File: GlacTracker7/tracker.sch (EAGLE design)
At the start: 79 parts, among them J1 THING_PLUS_PHYSICAL, J5 JST_6_PIN_VERTICAL, Q1 2N3906, Q2 AO6401A, Q3 DMN6070SY, U2 FONA-800-BREAKOUT, U3 MP2155GQ-Z, U4 SPARKFUN-SWARM-M138, U5 SPARKFUN-GPS-ZED-F9P, U6 MP2155GQ-Z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

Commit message: progress
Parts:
- removed J5: JST_6_PIN_VERTICAL, SparkFun-Connectors:JST_6_PIN_VERTICAL
- removed JP4, JP5, JP6, JP7: (no value), jumper:JP2E
- added C21: 1uF, resistor:C-EUC0805
- added JP8: (no value), jumper:JP1Q
- added Q6: MMBT3906LT1SMD, transistor-pnp:MMBT3906LT1SMD
- added Q7, Q8: DMG6602SVT, farnell-parts:DMG6602SVT
- added R20, R21, R23: 100k, SparkFun-Resistors:RESISTOR0603
- added R22, R26: 100K, resistor:R-EU_R0805
- added R24: 200R 0.1%, resistor:R-EU_R0805
- added R25: 1K 0.1%, resistor:R-EU_R0805
- added VCC_S: TPB2,54, testpad:TPB2,54
- Q2: value AO6401A -> DMG6602SVT; device GlacTracker:AO6401A -> farnell-parts:DMG6602SVT
- Q3: value DMN6070SY -> DMG6602SVT; device GlacTracker:DMN6070SY-13 -> farnell-parts:DMG6602SVT
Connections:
- removed net GPS_RX1: J1.A1, U5.RXI/MOSI
- removed net GPS_TX1: J1.A2, U5.TXO/MISO
- removed net GSM_EN: JP11.1, Q3.G, R19.1
- removed net GSM_PS: J1.GPIO0, U2.PS
- removed net GSM_RX: J1.A5, U2.RX
- removed net GSM_TX: J1.GPIO5, U2.TX
- removed net KEY: J1.GPIO1, U2.KEY
- removed net N$16: JP7.2, U6.EN
- removed net N$4: JP5.2, U3.EN
- removed net PSU_EN: J5.3, Q1.C, R2.2
- removed net SWARM_EN: J1.SCK, J5.1
- removed net SWARM_RX: J1.PICO, U4.RXI
- removed net SWARM_TX: J1.POCI, U4.TXO
- removed net VCC1_EN: J1.A0, J5.2, JP7.1
- removed net VCC_1: TP6.1
- new net +3V3: Q7G$2.S, R22.2
- new net ADC_7: C21.1, R24.2, R25.1
- new net BATV_EN: J1.A1
- new net BATV_IN: J1.A0
- new net COMMS_EN: J1.GPIO1, JP8.1, Q3G$1.G, R21.1, U6.EN, U6.MODE/SYNC
- new net COMMS_RX: J1.GPIO0, U2.RX, U4.RXI
- new net COMMS_TX: J1.GPIO5, U2.TX, U4.TXO
- new net GNDA: C21.2, R24.1
- new net GPS_EN: J1.FREE, JP11.1, Q2G$1.G, R19.1
- new net GSM_KEY: J1.GPIO6, U2.KEY
- new net N$35: Q3G$1.D@1, Q3G$2.G, R20.2
- new net SD_CS: J1.A5
- new net SD_MISO: J1.POCI
- new net SD_MOSI: J1.PICO
- new net SD_SCK: J1.SCK
- new net SENSE_3V3: Q7G$2.D, VCC_S.TP
- new net SENSE_EN: Q7G$1.G, Q8G$1.G
- new net SPARE: J1.A4
- new net SPARE2: J1.A3
- new net SPARE3: J1.A2
- new net VCC: Q8G$2.S, R26.2
- new net VCC_HP2_SW1: Q8G$2.D, R25.2
- new net V_COMMS_IO: Q3G$2.D, U2.V_IO
- new net V_GPS: C1.1, C5.1, C7.1, Q2G$2.D, U5.3V3, XB1.VCC
- net 3.3V: now also JP11.2, JP8.2, Q2G$2.S, Q3G$2.S, R18.1, R20.1; no longer C1.1, C5.1, C7.1, U2.V_IO, U5.3V3, XB1.VCC
- net 3V3_EN: now also Q1.C, Q6.C, R2.2, R23.1, U3.EN, U3.MODE/SYNC; no longer JP5.1
- net 4.4V: now also C10.+, C3.1, C9.+, TP6.1, U2.V_BAT, U4.VIN
- net GND: now also Q2G$1.S, Q3G$1.S, Q7G$1.S, Q8G$1.S, R21.2, R23.2; no longer JP4.1, JP6.1, Q3.S
- net N$1: now also Q7G$1.D@1, Q7G$2.G, R22.1; no longer Q1.B, R1.2
- net N$12: now also Q8G$1.D@1, Q8G$2.G, R26.1; no longer JP6.2, U6.MODE/SYNC
- net N$2: now also Q1.B, Q6.B, R1.2; no longer JP4.2, U3.MODE/SYNC
- net N$34: now also Q2G$1.D@1, Q2G$2.G; no longer Q2.G, Q3.D
- net RTC_BAT: now also Q6.E
- net SCL: now also U5.SCL/SCK
- net SDA: now also U5.SDA/!CS
- net V_GSM: no longer C10.+, C9.+, Q2.D, U2.V_BAT
- net V_SWARM: no longer C3.1, U4.VIN
- net V_SYS: no longer JP11.2, JP4.3, JP5.3, JP6.3, JP7.3, Q2.S, R18.1
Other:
- note added: "Bat Measure"
- note added: "GPS Enable"
- note removed: "3 - 3V3_EN 2 - VCC1_EN 1 - 5V_EN NOTE: On GlacTrackerPSU_V1, the enable connection labeled V_GSM (pin4) is no longer used to power the GSM module. Instead VCC1 is set to 4V and used to power GSM. See README/ report for more info"
- note removed: "GSM-ENABLE"
- moved on the sheet: BT1, C10, C16, C17, C18, C19, C2, C20, C3, C9, L3, R1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

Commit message: Complete board for checking and naming
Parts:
- removed JP11, JP8: (no value), jumper:JP1Q
- removed LED1, LED2, LED3: (no value), led:LEDCHIP-LED0805
- removed Q8: DMG6602SVT, farnell-parts:DMG6602SVT
- removed R23: 100k, SparkFun-Resistors:RESISTOR0603
- removed R26: 100K, resistor:R-EU_R0805
- removed TP5: TEST-POINTTP_15TH_THRU, SparkFun-Connectors:TEST-POINTTP_15TH_THRU
- removed VCC_S: TPB2,54, testpad:TPB2,54
- added 3.3V, 4.4V, GPS, GSM: (no value), led:LEDCHIP-LED0805
- added LED_EN: (no value), jumper:JP1Q
- added R27: 1k, SparkFun-Resistors:RESISTOR0603
- added U$1: ADAFRUIT-XTSD, GlacTracker:ADAFRUIT-XTSD
- JP1, JP2, JP3: value JUMPER-SMT_2_NC_TRACE_SILK -> (none); device SparkFun-Jumpers:JUMPER-SMT_2_NC_TRACE_SILK -> jumper:JP1Q
- R22: value 100K -> 100k; device resistor:R-EU_R0805 -> SparkFun-Resistors:RESISTOR0603
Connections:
- removed net +3V3: Q7G$2.S, R22.2
- removed net ADC_7: C21.1, R24.2, R25.1
- removed net GNDA: C21.2, R24.1
- removed net N$1: Q7G$1.D@1, Q7G$2.G, R22.1
- removed net N$6: JP1.2, LED1.C
- removed net N$7: JP2.2, LED2.C
- removed net N$8: JP3.2, LED3.C
- removed net SENSE_3V3: Q7G$2.D, VCC_S.TP
- removed net SENSE_EN: Q7G$1.G, Q8G$1.G
- removed net VCC: Q8G$2.S, R26.2
- removed net VCC_2: TP5.1
- removed net V_GSM: R4.2
- removed net V_SWARM: R5.2
- new net N$3: 3.3V.C, 4.4V.C, GPS.C, GSM.C, LED_EN.2
- new net N$4: GPS.A, R4.1
- net 3.3V: now also JP2.2, JP3.2, U$1.3.3V; no longer C6.1, C8.1, JP11.2, JP8.2
- net 3V3_EN: now also JP1.1; no longer R23.1
- net 4.4V: now also R5.2
- net BATV_EN: now also Q7G$1.G
- net BATV_IN: now also C21.1, R24.2, R25.1
- net COMMS_EN: now also JP2.1; no longer JP8.1
- net GND: now also C21.2, J1.GND, LED_EN.1, R24.1, U$1.GND; no longer JP1.1, JP2.1, JP3.1, Q8G$1.S, R23.2
- net GPS_EN: now also JP3.1; no longer JP11.1
- net N$12: now also Q7G$1.D@1, Q7G$2.G, R22.2; no longer Q8G$1.D@1, Q8G$2.G, R26.1
- net N$13: now also 3.3V.A; no longer LED1.A
- net N$14: now also GSM.A, R27.1; no longer LED2.A, R4.1
- net N$15: now also 4.4V.A; no longer LED3.A
- net SD_CS: now also U$1.CS
- net SD_MISO: now also U$1.MISO
- net SD_MOSI: now also U$1.MOSI
- net SD_SCK: now also U$1.SCK
- net VCC_HP2_SW1: now also Q7G$2.D; no longer Q8G$2.D
- net V_BATT: now also Q7G$2.S, R22.1
- net V_COMMS_IO: now also R27.2
- net V_GPS: now also C6.1, C8.1, R4.2
- net V_SYS: now also JP1.2
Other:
- note removed: "Bat Measure"
- note removed: "Connectors"

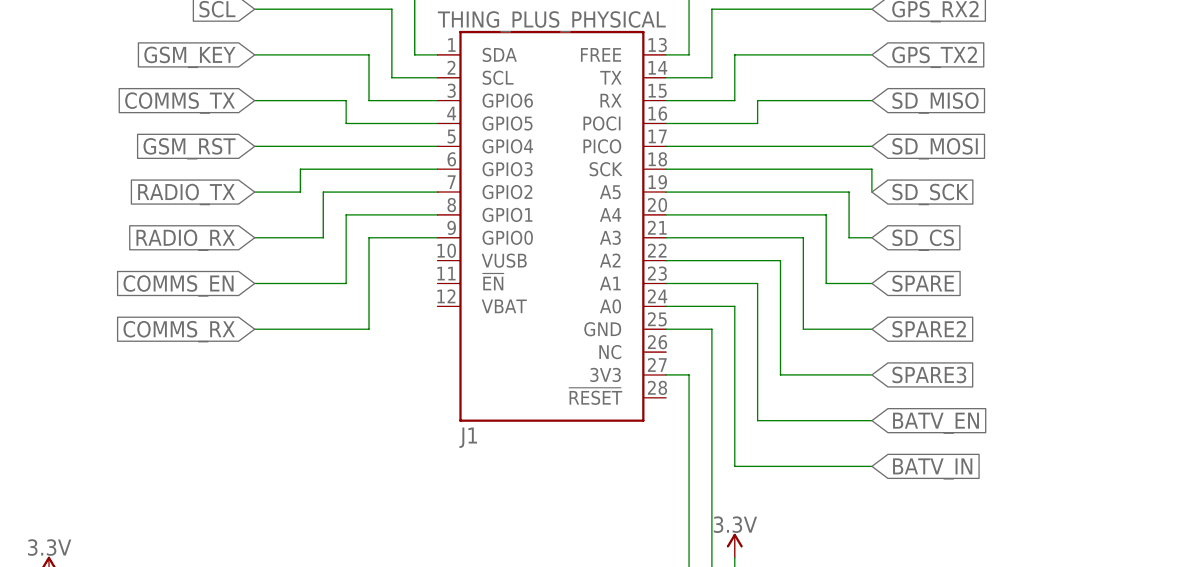
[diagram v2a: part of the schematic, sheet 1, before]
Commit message: DRCand ERC run. Some tweaks to make to the Swarm/GSMoverlap
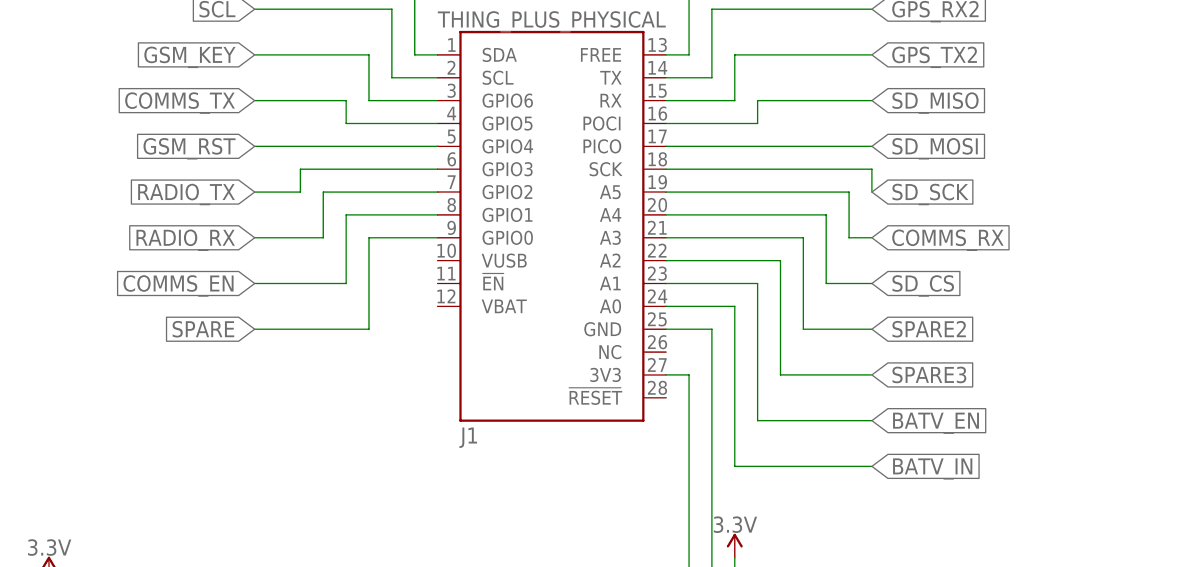
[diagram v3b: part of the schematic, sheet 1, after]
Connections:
- net COMMS_RX: now also J1.A5; no longer J1.GPIO0
- net SD_CS: now also J1.A4; no longer J1.A5
- net SPARE: now also J1.GPIO0; no longer J1.A4
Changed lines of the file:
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@@
 <net name="SD_CS" class="0">
-<segment>
-<label x="109.22" y="137.16" size="1.778" layer="95" xref="yes"/>
-<pinref part="J1" gate="G$1" pin="A5"/>
-<wire x1="86.36" y1="142.24" x2="106.68" y2="142.24" width="0.1524" layer="91"/>
-<wire x1="106.68" y1="142.24" x2="106.68" y2="137.16" width="0.1524" layer="91"/>
-<wire x1="106.68" y1="137.16" x2="109.22" y2="137.16" width="0.1524" layer="91"/>
-</segment>
 <segment>
 <label x="55.88" y="78.74" size="1.778" layer="95" xref="yes"/>
 <pinref part="U$1" gate="G$1" pin="CS"/>
 <wire x1="50.8" y1="78.74" x2="55.88" y2="78.74" width="0.1524" layer="91"/>
+</segment>
+<segment>
+<label x="109.22" y="132.08" size="1.778" layer="95" xref="yes"/>
+<pinref part="J1" gate="G$1" pin="A4"/>
+<wire x1="86.36" y1="139.7" x2="104.14" y2="139.7" width="0.1524" layer="91"/>
+<wire x1="104.14" y1="139.7" x2="104.14" y2="132.08" width="0.1524" layer="91"/>
+<wire x1="104.14" y1="132.08" x2="109.22" y2="132.08" width="0.1524" layer="91"/>
 </segment>
 </net>
@@
 <net name="COMMS_RX" class="0">
 <segment>
-<label x="40.64" y="127" size="1.778" layer="95" rot="R180" xref="yes"/>
-<pinref part="J1" gate="G$1" pin="GPIO0"/>
-<wire x1="40.64" y1="127" x2="53.34" y2="127" width="0.1524" layer="91"/>
-<wire x1="53.34" y1="127" x2="53.34" y2="137.16" width="0.1524" layer="91"/>
-<wire x1="53.34" y1="137.16" x2="60.96" y2="137.16" width="0.1524" layer="91"/>
+<label x="109.22" y="137.16" size="1.778" layer="95" xref="yes"/>
+<pinref part="J1" gate="G$1" pin="A5"/>
+<wire x1="86.36" y1="142.24" x2="106.68" y2="142.24" width="0.1524" layer="91"/>
+<wire x1="106.68" y1="142.24" x2="106.68" y2="137.16" width="0.1524" layer="91"/>
+<wire x1="106.68" y1="137.16" x2="109.22" y2="137.16" width="0.1524" layer="91"/>
 </segment>
 </net>
@@
 </segment>
 </net>
-<net name="SPARE" class="0">
-<segment>
-<label x="109.22" y="132.08" size="1.778" layer="95" xref="yes"/>
-<pinref part="J1" gate="G$1" pin="A4"/>
-<wire x1="86.36" y1="139.7" x2="104.14" y2="139.7" width="0.1524" layer="91"/>
-<wire x1="104.14" y1="139.7" x2="104.14" y2="132.08" width="0.1524" layer="91"/>
-<wire x1="104.14" y1="132.08" x2="109.22" y2="132.08" width="0.1524" layer="91"/>
-</segment>
-</net>
 <net name="SPARE2" class="0">
 <segment>
@@
 </segment>
 </net>
+<net name="SPARE" class="0">
+<segment>
+<label x="40.64" y="127" size="1.778" layer="95" rot="R180" xref="yes"/>
+<pinref part="J1" gate="G$1" pin="GPIO0"/>
+<wire x1="40.64" y1="127" x2="53.34" y2="127" width="0.1524" layer="91"/>
+<wire x1="53.34" y1="127" x2="53.34" y2="137.16" width="0.1524" layer="91"/>
+<wire x1="53.34" y1="137.16" x2="60.96" y2="137.16" width="0.1524" layer="91"/>
+</segment>
+</net>

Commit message: missed and airwire
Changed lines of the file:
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@@
 <label x="40.64" y="142.24" size="1.778" layer="95" rot="R180" xref="yes"/>
 <pinref part="J1" gate="G$1" pin="GPIO3"/>
-<wire x1="40.64" y1="142.24" x2="45.72" y2="142.24" width="0.1524" layer="91"/>
-<wire x1="45.72" y1="142.24" x2="45.72" y2="144.78" width="0.1524" layer="91"/>
-<wire x1="45.72" y1="144.78" x2="60.96" y2="144.78" width="0.1524" layer="91"/>
+<wire x1="40.64" y1="142.24" x2="50.8" y2="142.24" width="0.1524" layer="91"/>
+<wire x1="50.8" y1="142.24" x2="50.8" y2="144.78" width="0.1524" layer="91"/>
+<wire x1="50.8" y1="144.78" x2="60.96" y2="144.78" width="0.1524" layer="91"/>
 </segment>
 </net>
@@
 <label x="40.64" y="137.16" size="1.778" layer="95" rot="R180" xref="yes"/>
 <pinref part="J1" gate="G$1" pin="GPIO2"/>
-<wire x1="40.64" y1="137.16" x2="48.26" y2="137.16" width="0.1524" layer="91"/>
-<wire x1="48.26" y1="137.16" x2="48.26" y2="142.24" width="0.1524" layer="91"/>
-<wire x1="48.26" y1="142.24" x2="60.96" y2="142.24" width="0.1524" layer="91"/>
+<wire x1="40.64" y1="137.16" x2="53.34" y2="137.16" width="0.1524" layer="91"/>
+<wire x1="53.34" y1="137.16" x2="53.34" y2="142.24" width="0.1524" layer="91"/>
+<wire x1="53.34" y1="142.24" x2="60.96" y2="142.24" width="0.1524" layer="91"/>
 </segment>
 </net>
@@
 <label x="40.64" y="132.08" size="1.778" layer="95" rot="R180" xref="yes"/>
 <pinref part="J1" gate="G$1" pin="GPIO1"/>
-<wire x1="40.64" y1="132.08" x2="50.8" y2="132.08" width="0.1524" layer="91"/>
-<wire x1="50.8" y1="132.08" x2="50.8" y2="139.7" width="0.1524" layer="91"/>
-<wire x1="50.8" y1="139.7" x2="60.96" y2="139.7" width="0.1524" layer="91"/>
+<wire x1="40.64" y1="132.08" x2="55.88" y2="132.08" width="0.1524" layer="91"/>
+<wire x1="55.88" y1="132.08" x2="55.88" y2="139.7" width="0.1524" layer="91"/>
+<wire x1="55.88" y1="139.7" x2="60.96" y2="139.7" width="0.1524" layer="91"/>
 </segment>
 </net>
@@
 <label x="40.64" y="127" size="1.778" layer="95" rot="R180" xref="yes"/>
 <pinref part="J1" gate="G$1" pin="GPIO0"/>
-<wire x1="40.64" y1="127" x2="53.34" y2="127" width="0.1524" layer="91"/>
-<wire x1="53.34" y1="127" x2="53.34" y2="137.16" width="0.1524" layer="91"/>
-<wire x1="53.34" y1="137.16" x2="60.96" y2="137.16" width="0.1524" layer="91"/>
+<wire x1="40.64" y1="127" x2="58.42" y2="127" width="0.1524" layer="91"/>
+<wire x1="58.42" y1="127" x2="58.42" y2="137.16" width="0.1524" layer="91"/>
+<wire x1="58.42" y1="137.16" x2="60.96" y2="137.16" width="0.1524" layer="91"/>
 </segment>
 </net>
@@
 <wire x1="220.98" y1="99.06" x2="220.98" y2="96.52" width="0.1524" layer="91"/>
 <wire x1="220.98" y1="96.52" x2="213.36" y2="96.52" width="0.1524" layer="91"/>
-<junction x="220.98" y="96.52"/>
-<wire x1="220.98" y1="93.98" x2="220.98" y2="96.52" width="0.1524" layer="91"/>
 <wire x1="213.36" y1="96.52" x2="205.74" y2="96.52" width="0.1524" layer="91"/>
+<junction x="205.74" y="96.52"/>
+<junction x="213.36" y="96.52"/>
 </segment>
 </net>
@@
 </sheet>
 </sheets>
+<errors>
+</errors>
 </schematic>
 </drawing>

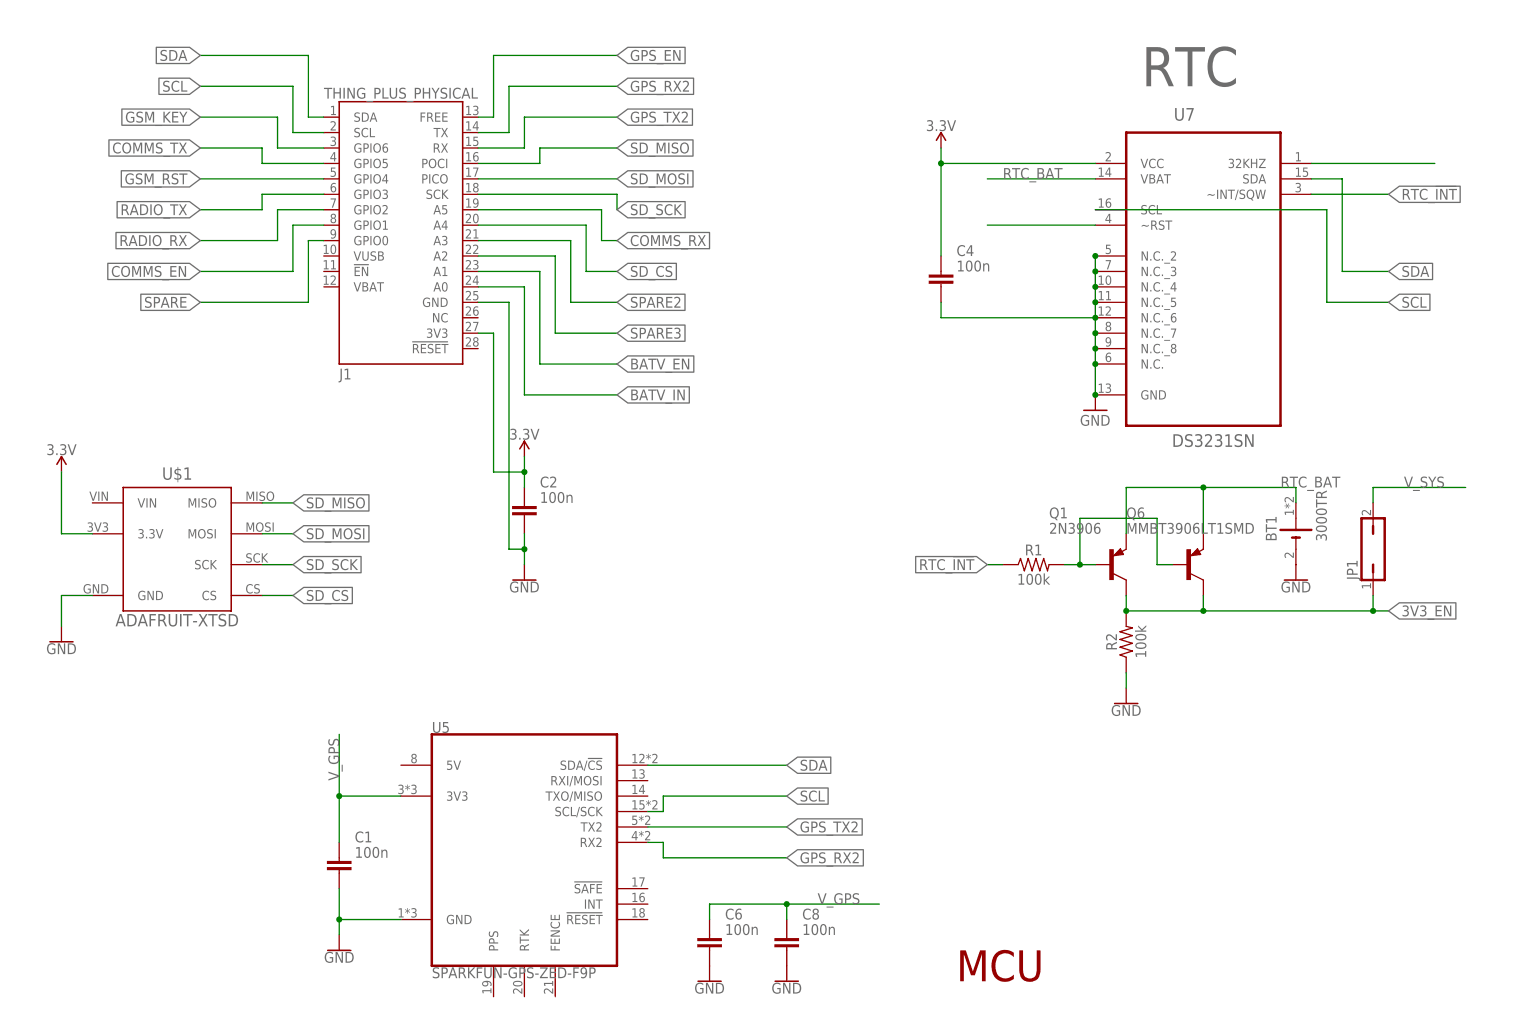
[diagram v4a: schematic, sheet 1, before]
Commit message: Added accelerometer
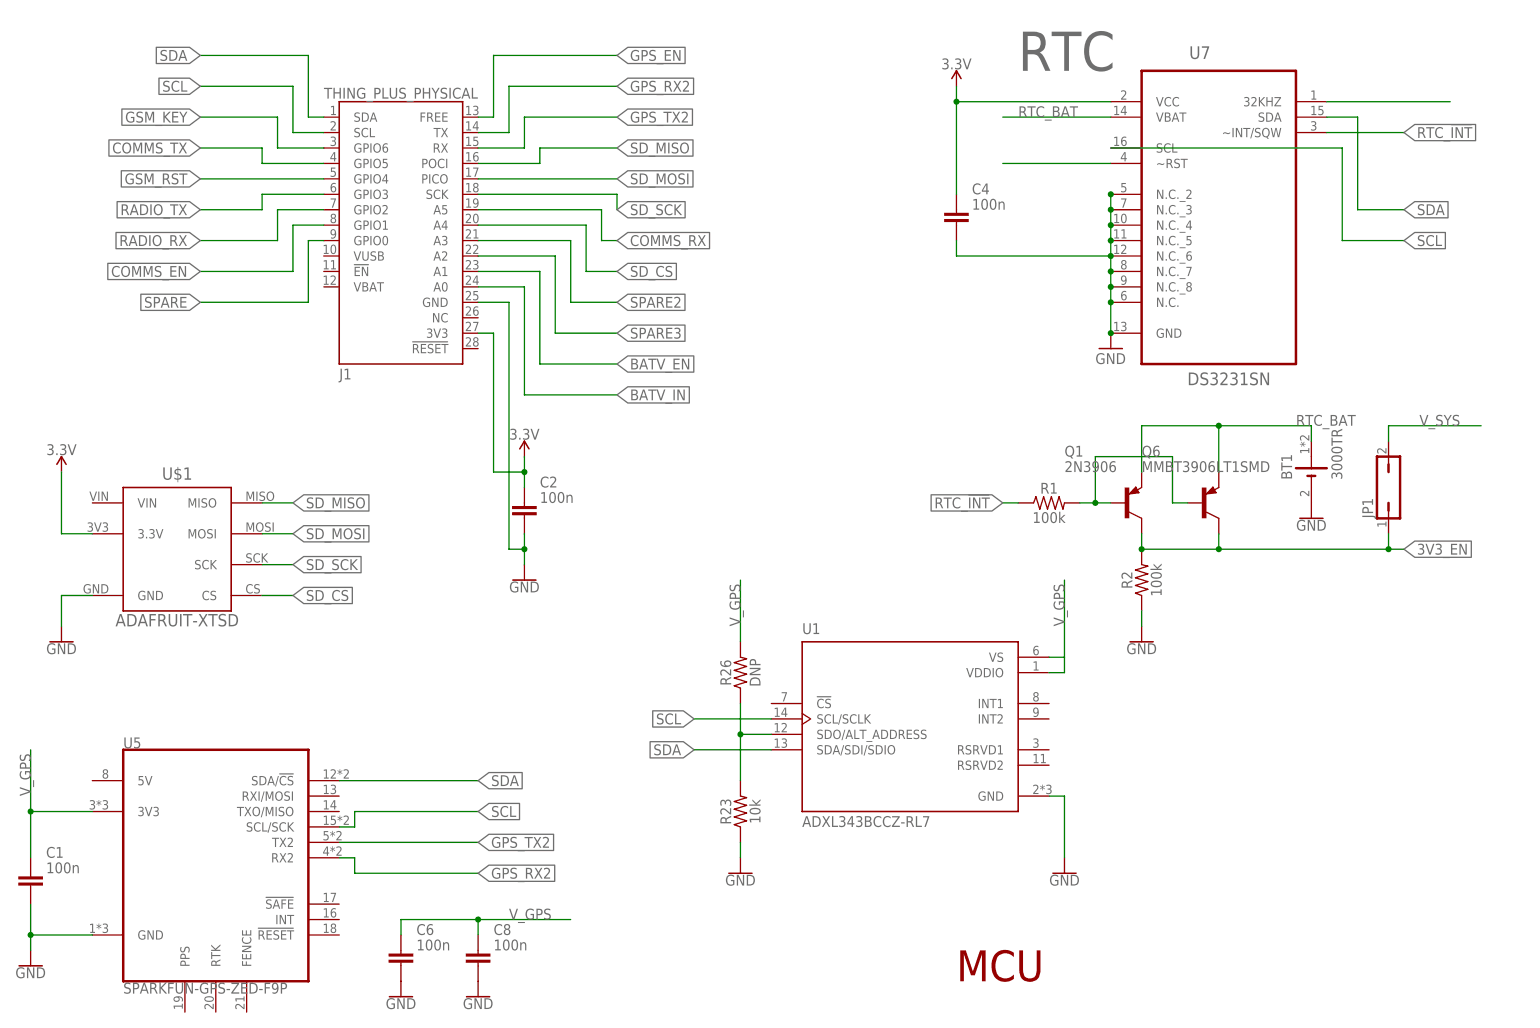
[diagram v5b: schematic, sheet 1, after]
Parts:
- added R23: 10k, SparkFun-Resistors:RESISTOR0603
- added R26: DNP, SparkFun-Resistors:RESISTOR0603
- added U1: ADXL343BCCZ-RL7, GlacTracker:ADXL343BCCZ-RL7
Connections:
- new net N$1: R23.2, R26.1, U1.SDO/ALT_ADDRESS
- net GND: now also R23.1, U1.GND
- net SCL: now also U1.SCL/SCLK
- net SDA: now also U1.SDA/SDI/SDIO
- net V_GPS: now also R26.2, U1.VDDIO, U1.VS
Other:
- moved on the sheet: BT1, C1, C4, C6, C8, JP1, Q1, Q6, R1, R2, U5, U7
